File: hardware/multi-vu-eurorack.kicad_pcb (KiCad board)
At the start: 2 copper layers, 131 parts, among them IC1 LM4040DBZ-10, IC2 ATtiny85, IC3 74HC595, IC4 74HC595, J1 AudioJack2_SwitchT, J2 EURO_HEADER_10pin, J3 AVR-ISP-6, J4 AudioJack2_SwitchT, J5 AudioJack2_SwitchT, J6 AudioJack2_SwitchT, J7 AudioJack2_SwitchT, SW1 EVQQ2, U1 TL074, U2 TLV172IDCK, U3 MCP6001-OT, U4 L78L05_SOT89

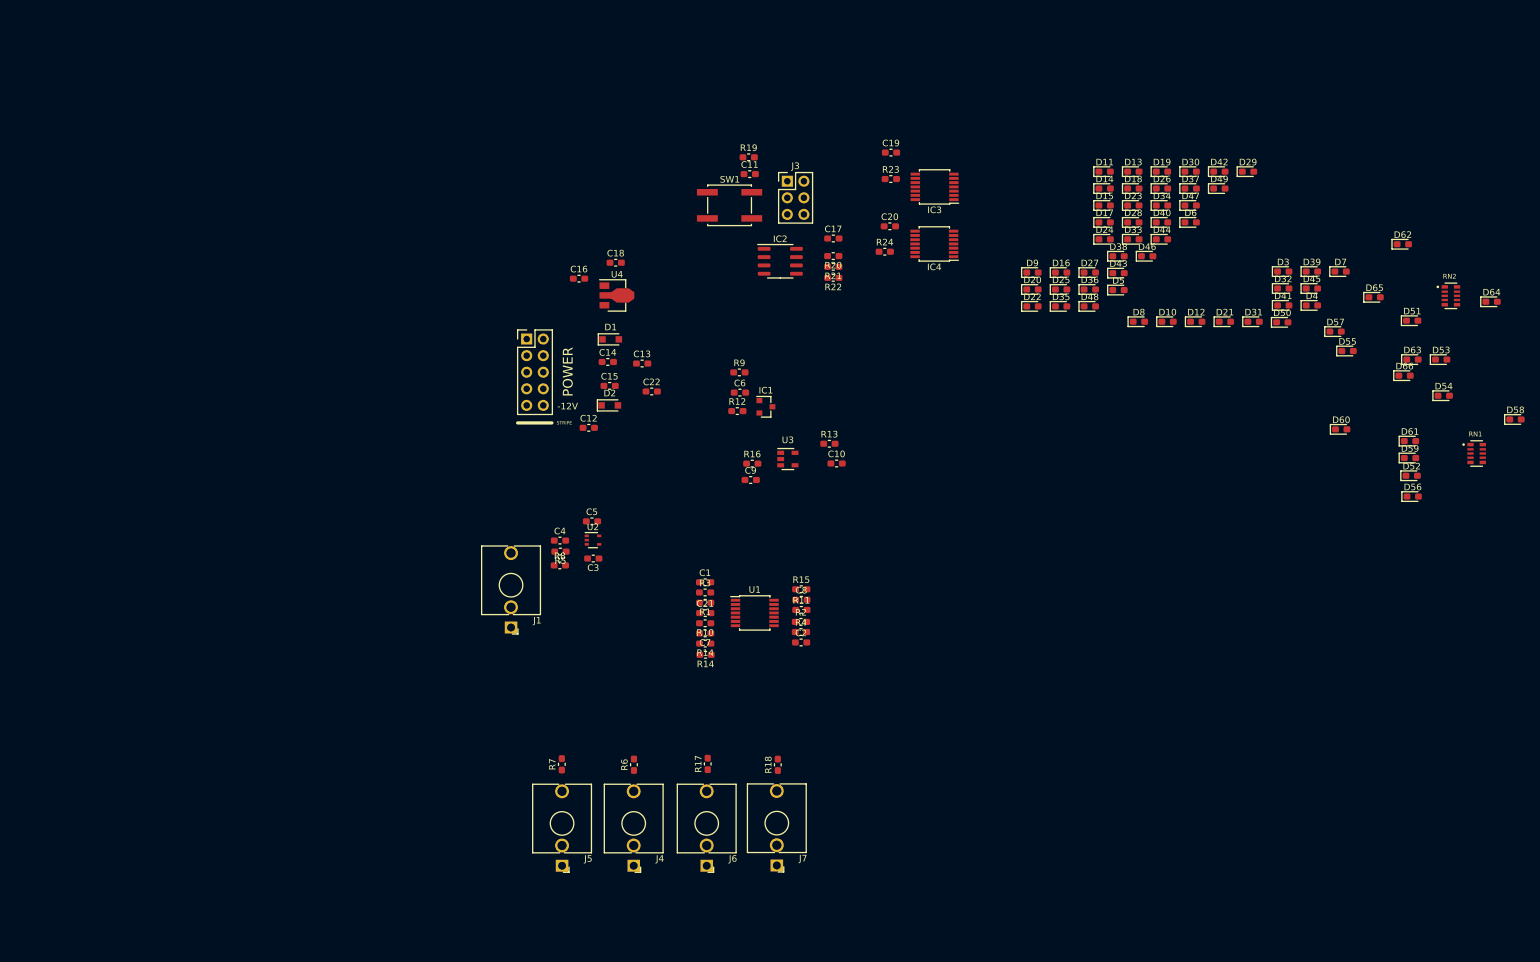
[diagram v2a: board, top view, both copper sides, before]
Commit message: Separated and arranged passives around mainboard ICs, started arranging LEDs on panel reverse.
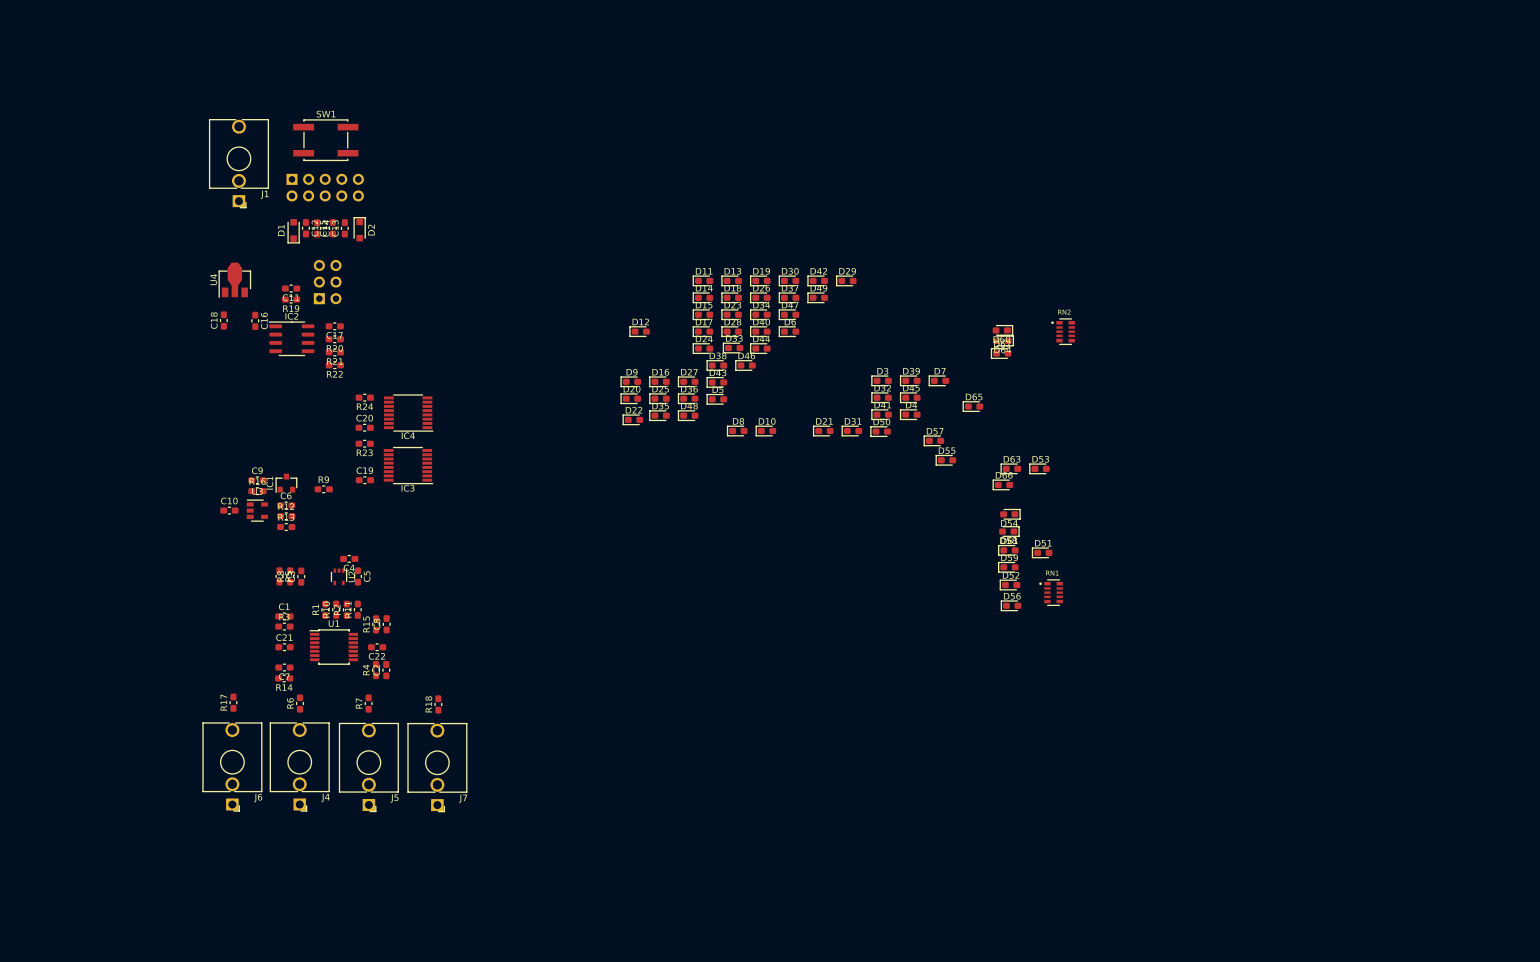
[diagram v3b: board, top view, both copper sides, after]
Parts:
- removed the R14 at (131.8, 119.0)
- removed the R14 at (131.7, 117.3)
- added R14: 100k, Capacitor_SMD:C_0603_1608Metric_Pad1.05x0.95mm_HandSolder, F.Cu at (67.3, 122.6)
- IC3, IC4: footprint Package_SO:TSSOP-14_4.4x5mm_P0.65mm -> Package_SO:TSSOP-16_4.4x5mm_P0.65mm
- J2, J3: moved to B.Cu
- moved C19 94.9 mm to (79.6, 92.3)
- moved C10 93.2 mm to (58.9, 96.9)
- moved IC3 91.2 mm to (86.2, 90.0)
- moved R23 90.2 mm to (79.6, 86.7), turned to 180 degrees
- moved C20 86.1 mm to (79.6, 84.3)
- moved D12 85.1 mm to (121.9, 69.5)
- moved IC4 84.6 mm to (86.2, 82.0)
- moved R13 84.1 mm to (67.6, 99.5)
- moved R24 82.7 mm to (79.6, 79.7), turned to 180 degrees
- moved U3 81.6 mm to (63.2, 97.0)
- moved D58 79.5 mm to (178.1, 100.2), turned to 180 degrees
- moved C17 77.5 mm to (75.0, 68.7), turned to 180 degrees
- moved R22 77.5 mm to (75.0, 74.7)
- moved J1 77.4 mm to (60.3, 49.6)
- moved R21 77.4 mm to (75.0, 72.7)
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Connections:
- D11 pad 2: (no net) -> Net-(D11-Pad2)
- D3 pad 2: (no net) -> Net-(D3-Pad2)
- R23 pad 1: +5V -> Net-(IC3-Pad10)
- R23 pad 2: Net-(IC3-Pad10) -> +5V
- R24 pad 1: +5V -> Net-(IC4-Pad10)
- R24 pad 2: Net-(IC4-Pad10) -> +5V

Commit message: finalized the rough placements of the component subcircuit groups.  Added traces between analog circuits for multiple subcircuit.
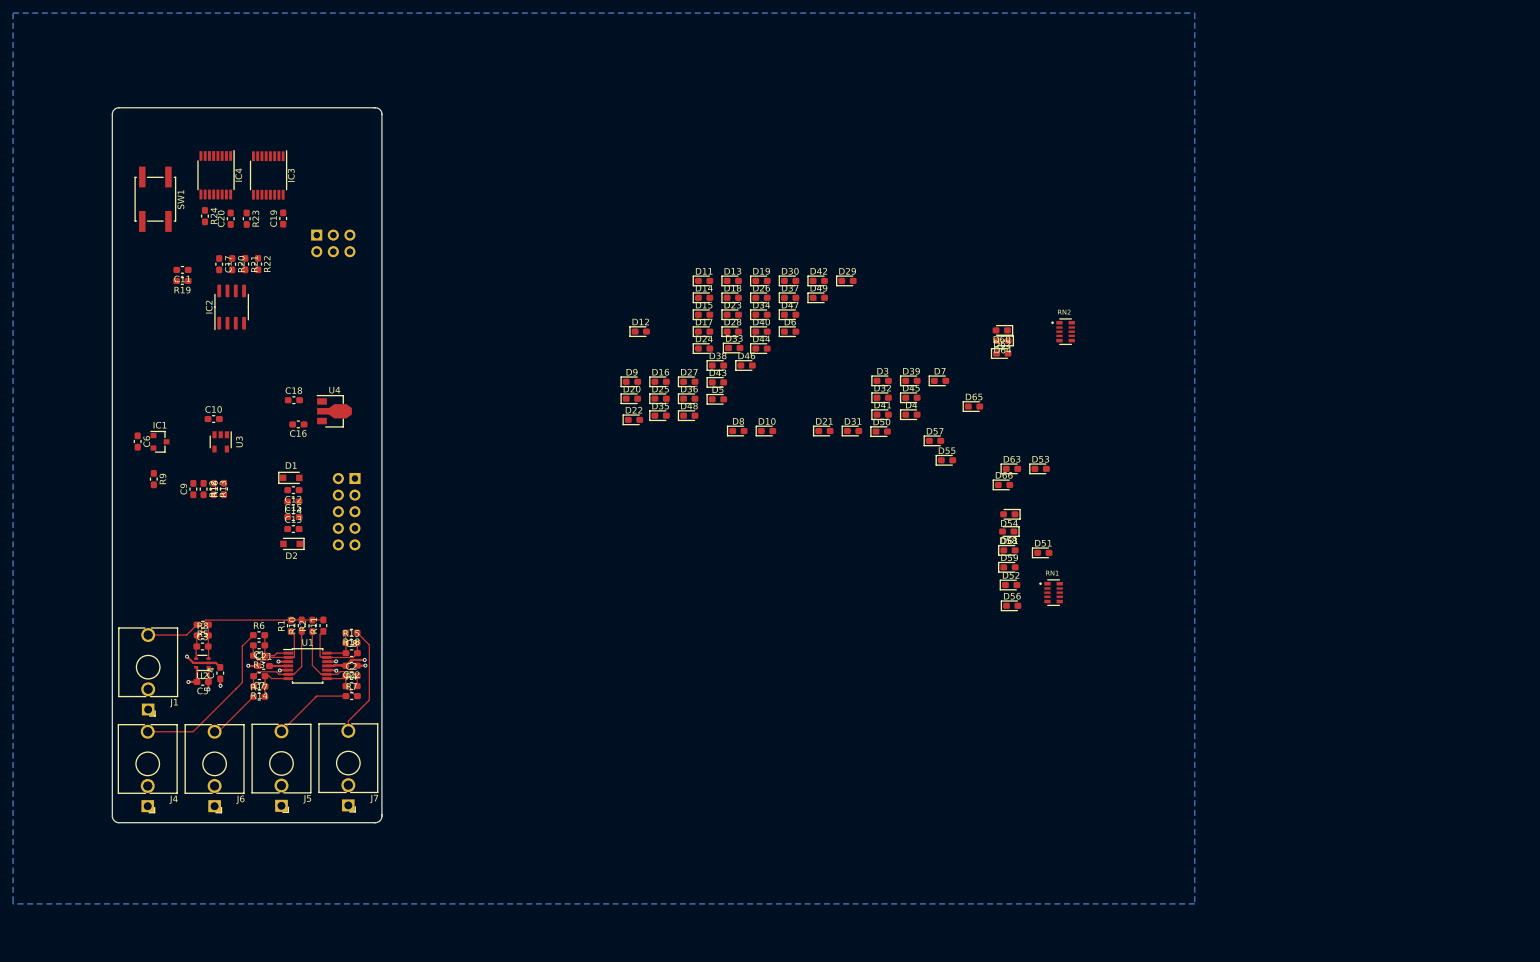
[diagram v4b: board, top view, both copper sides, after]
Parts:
- moved J1 79.1 mm to (46.4, 127.4)
- moved J2 52.1 mm to (73.3, 102.8), turned to 180 degrees
- moved IC3 49.3 mm to (64.8, 45.6), turned to 270 degrees
- moved D2 49.2 mm to (68.4, 102.0), turned to 180 degrees
- moved IC4 46.8 mm to (56.8, 45.6), turned to 270 degrees
- moved C13 46.7 mm to (68.7, 99.8), turned to 0 degrees
- moved C15 44.6 mm to (68.7, 97.9), turned to 0 degrees
- moved C19 42.0 mm to (67.1, 52.2), turned to 90 degrees
- moved C14 42.0 mm to (68.7, 95.6), turned to 180 degrees
- moved C12 40.1 mm to (68.7, 93.8), turned to 180 degrees
- moved R23 38.9 mm to (61.5, 52.3), turned to 270 degrees
- moved C20 38.0 mm to (59.1, 52.3), turned to 90 degrees
- moved D1 37.9 mm to (68.3, 91.9), turned to 0 degrees
- moved R24 37.0 mm to (55.1, 51.9), turned to 270 degrees
- moved C5 28.7 mm to (54.8, 123.2), turned to 180 degrees
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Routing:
- net /OUTA: track 0.00 -> 25.6 mm
- net /MULT_INPUT: track 0.00 -> 24.5 mm
- net /OUTD: track 0.00 -> 17.1 mm
- net Net-(C7-Pad2): track 0.00 -> 15.3 mm
- net Net-(C2-Pad2): track 0.00 -> 14.6 mm
- net GND: track 0.00 -> 13.0 mm, vias 0 -> 8
- net Net-(C1-Pad2): track 0.00 -> 12.4 mm
- net /OUTC: track 0.00 -> 12.3 mm
- net Net-(C8-Pad2): track 0.00 -> 11.7 mm
- net -12V: track 0.00 -> 9.84 mm, vias 0 -> 2
- net +12V: track 0.00 -> 8.68 mm, vias 0 -> 1
- net /OUTB: track 0.00 -> 8.18 mm
- net /INPUT: track 0.00 -> 8.13 mm
- net Net-(C2-Pad1): track 0.00 -> 7.89 mm
- net Net-(C1-Pad1): track 0.00 -> 6.90 mm
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- added copper zone on B.Cu, net GND
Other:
- board outline added: 41.3 x 109.5 mm
- net class Default: clearance 0.2 -> 0.127; trace_width 0.25 -> 0.127; via_dia 0.8 -> 0.4; via_drill 0.4 -> 0.2
- net class Power added: clearance 0.127, trace_width 0.35, via_dia 0.6, via_drill 0.3
- rule trace_clearance: 0.2 -> 0.127
- rule trace_min: 0.2 -> 0.127
- rule via_min_drill: 0.3 -> 0.2
